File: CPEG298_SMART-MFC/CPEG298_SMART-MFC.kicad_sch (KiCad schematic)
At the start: 4 parts, among them J1 Power, J2 Digital/PWM, J3 Analog, J4 Digital/PWM

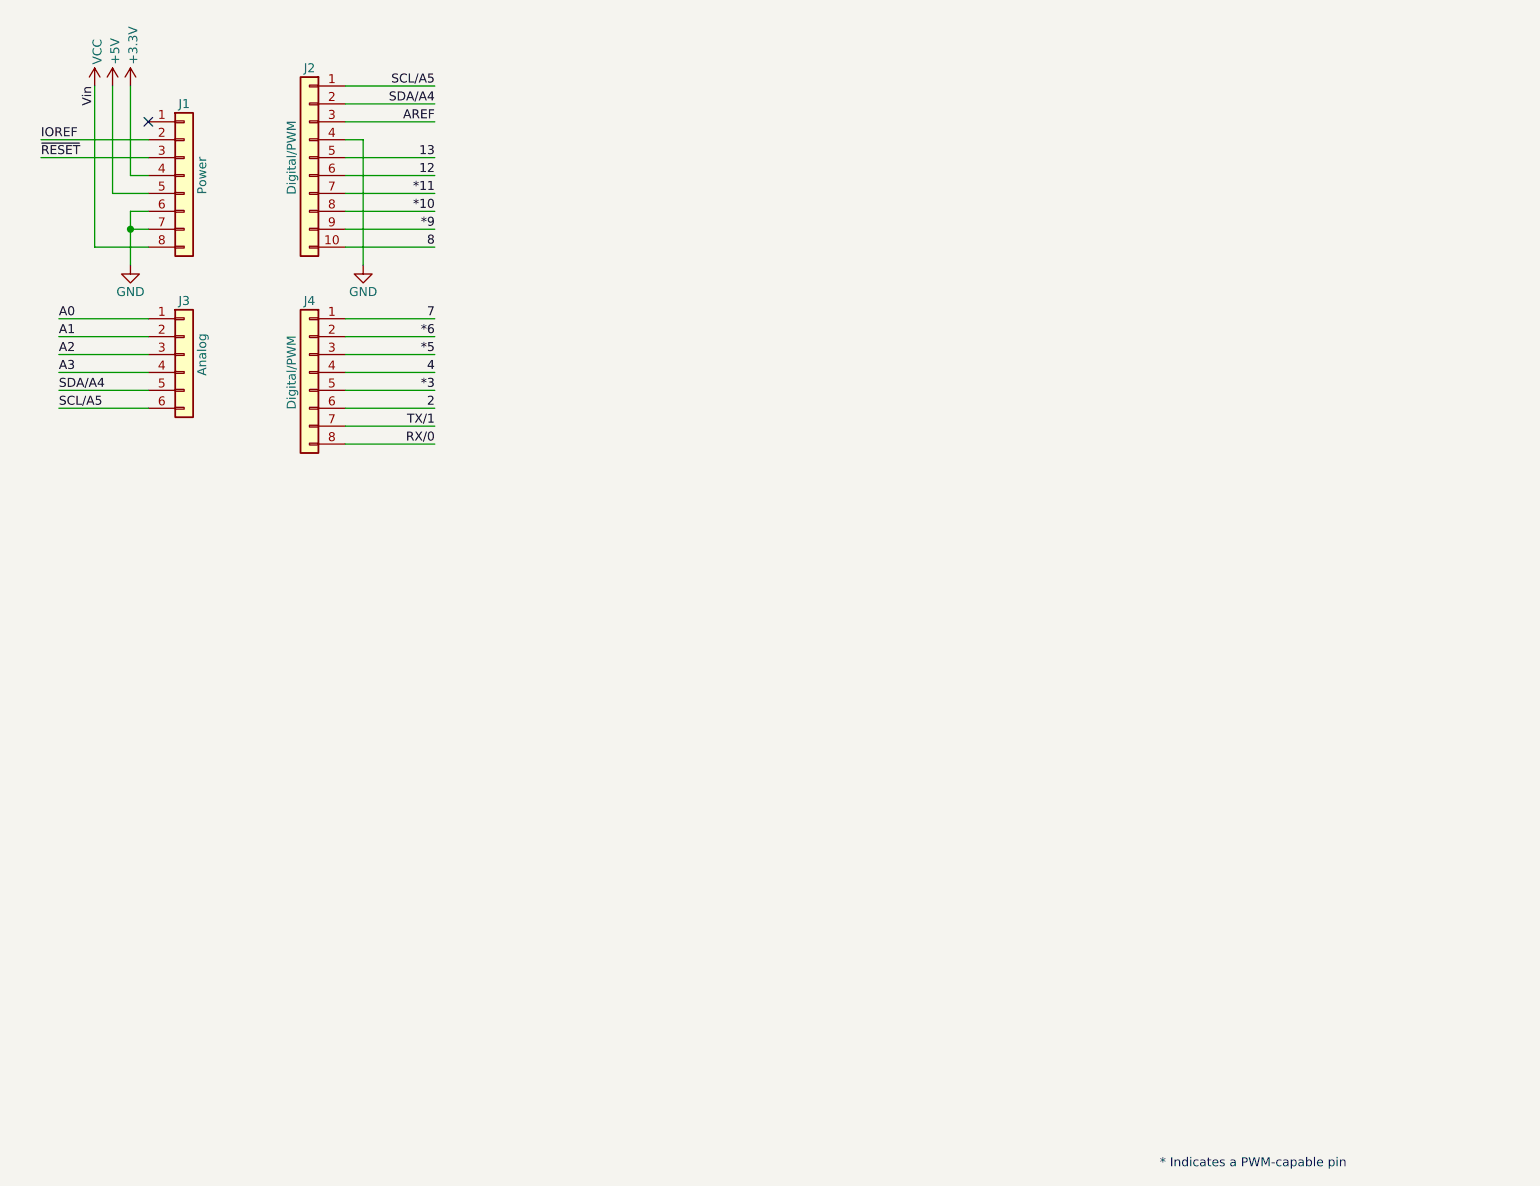
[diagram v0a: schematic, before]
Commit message: KiCad & Code
-Labeling on PCB
-Preparing code for millivolt reader
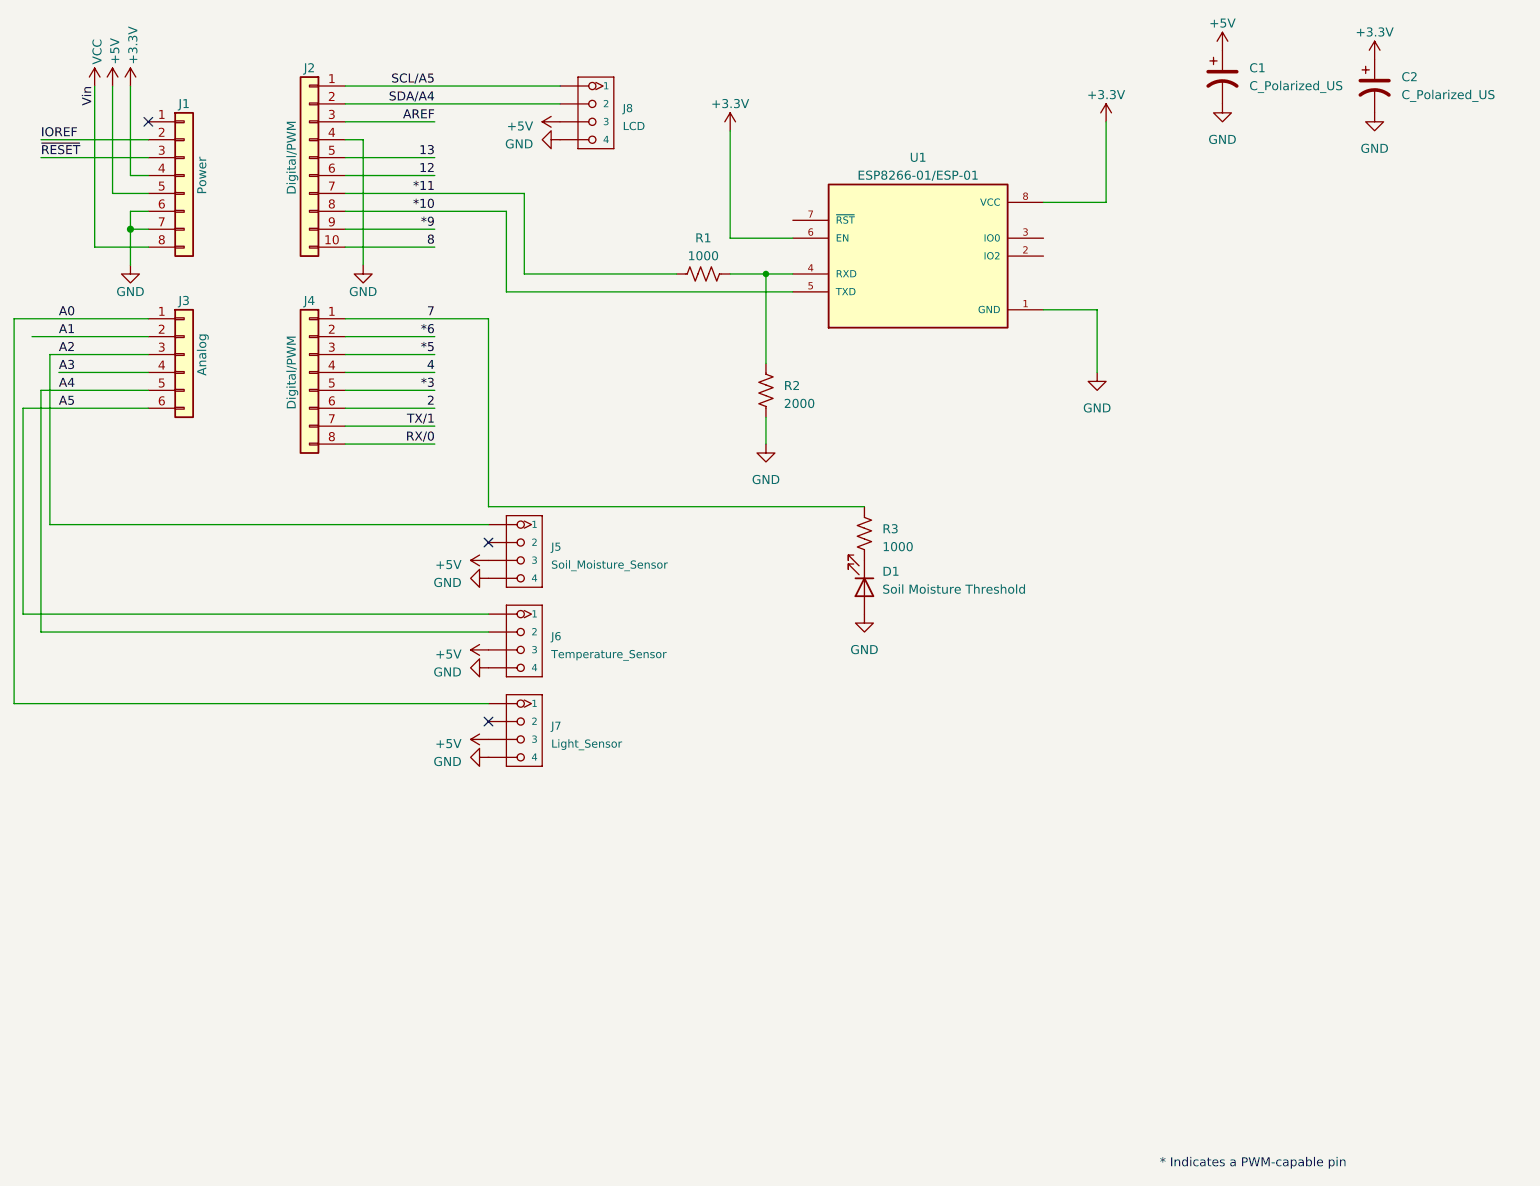
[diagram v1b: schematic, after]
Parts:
- added C1, C2: C_Polarized_US, Capacitor_THT:CP_Radial_D6.3mm_P2.50mm, symbol Device:C_Polarized_US
- added D1: Soil Moisture Threshold, LED_THT:LED_D5.0mm, symbol Device:LED
- added J5: Soil_Moisture_Sensor, OPL_Connector:HW4-2.0, symbol OPL_Connector:GROVE-CONNECTOR-DIP_4P-2.0_
- added J6: Temperature_Sensor, OPL_Connector:HW4-2.0, symbol OPL_Connector:GROVE-CONNECTOR-DIP_4P-2.0_
- added J7: Light_Sensor, OPL_Connector:HW4-2.0, symbol OPL_Connector:GROVE-CONNECTOR-DIP_4P-2.0_
- added J8: LCD, OPL_Connector:HW4-2.0, symbol OPL_Connector:GROVE-CONNECTOR-DIP_4P-2.0_
- added R1, R3: 1000, Resistor_THT:R_Axial_DIN0207_L6.3mm_D2.5mm_P10.16mm_Horizontal, symbol Device:R_US
- added R2: 2000, Resistor_THT:R_Axial_DIN0207_L6.3mm_D2.5mm_P10.16mm_Horizontal, symbol Device:R_US
- added U1: ESP8266-01/ESP-01, ESP8266-01_ESP-01:XCVR_ESP8266-01_ESP-01, symbol ESP8266-01_ESP-01:ESP8266-01/ESP-01
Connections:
- net *10: now also U1.5 (TXD)
- net *11: now also R1.1
- net +5V: now also C1.1, J5.3, J6.3, J7.3, J8.3
- net 7: now also R3.1
- net A0: now also J7.1
- net A2: now also J5.1
- net GND: now also C1.2, C2.2, D1.2 (A), J5.4, J6.4, J7.4, J8.4, R2.2, U1.1 (GND)
- net SCL/A5: now also J8.1; no longer J3.6 (Pin_6)
- net SDA/A4: now also J8.2; no longer J3.5 (Pin_5)
- new net: R1.2, R2.1, U1.4 (RXD)
- new net: D1.1 (K), R3.2
- new net +3.3V: C2.1, U1.6 (EN), U1.8 (VCC)
- new net A4: J3.5 (Pin_5), J6.2
- new net A5: J3.6 (Pin_6), J6.1
- no-connect marks 1 -> 3
